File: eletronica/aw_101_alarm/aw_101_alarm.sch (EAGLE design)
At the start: 40 parts, among them IC1 ATTINY2313V, IC2 4511N, J1 DCJ0202, T1 2N2222, T2 2N2222, T3 2N2222, T4 2N2222, T5 2N2222, T6 2N2222, X1 UPDOWN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

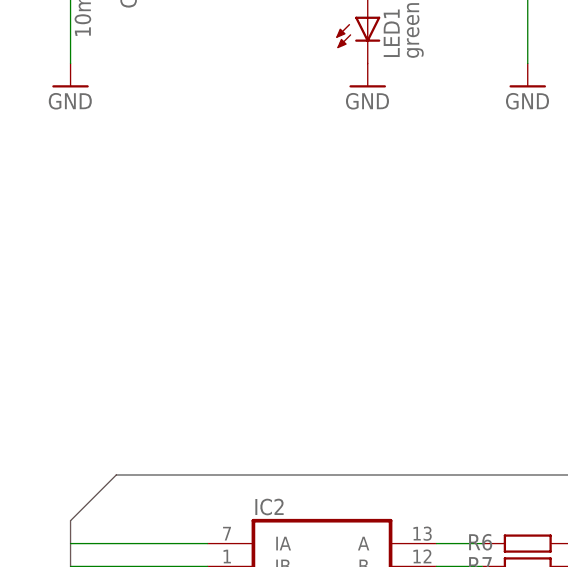
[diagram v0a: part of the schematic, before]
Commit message: 
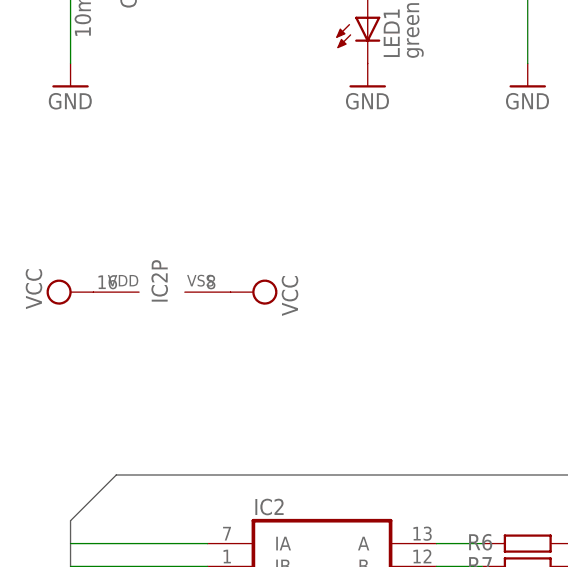
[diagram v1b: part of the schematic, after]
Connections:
- net VCC: now also IC2P.VDD, IC2P.VSS
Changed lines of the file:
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@@
 <part name="R17" library="rcl" deviceset="R-EU_" device="0207/10" value="1K"/>
 <part name="GND9" library="supply1" deviceset="GND" device=""/>
+<part name="SUPPLY3" library="supply2" deviceset="VCC" device=""/>
+<part name="SUPPLY4" library="supply2" deviceset="VCC" device=""/>
 </parts>
 <sheets>
@@
 <instance part="R17" gate="G$1" x="167.64" y="-66.04" rot="R180"/>
 <instance part="GND9" gate="1" x="177.8" y="-86.36"/>
+<instance part="IC2" gate="P" x="10.16" y="17.78" rot="R90"/>
+<instance part="SUPPLY3" gate="G$1" x="0" y="17.78" rot="R90"/>
+<instance part="SUPPLY4" gate="G$1" x="20.32" y="17.78" rot="R270"/>
 </instances>
 <busses>
@@
 <junction x="12.7" y="-22.86"/>
 </segment>
+<segment>
+<pinref part="IC2" gate="P" pin="VDD"/>
+<pinref part="SUPPLY3" gate="G$1" pin="VCC"/>
+</segment>
+<segment>
+<pinref part="IC2" gate="P" pin="VSS"/>
+<pinref part="SUPPLY4" gate="G$1" pin="VCC"/>
+</segment>
 </net>

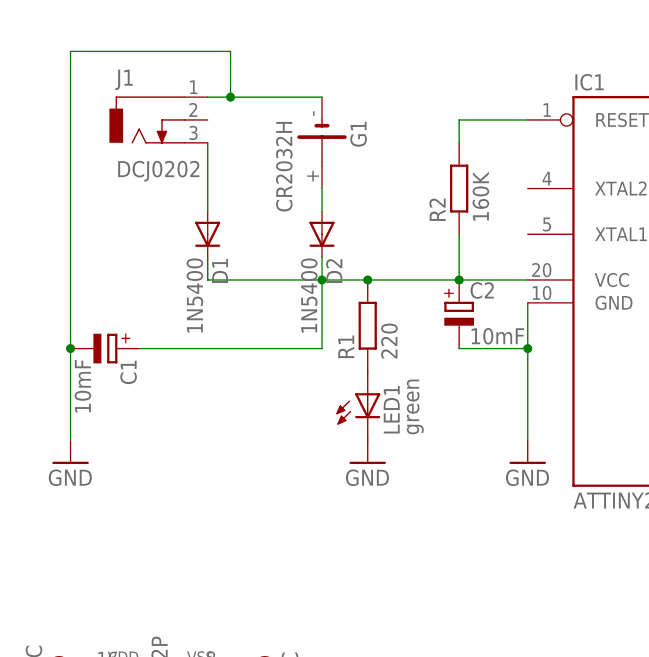
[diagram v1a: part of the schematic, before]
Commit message: 
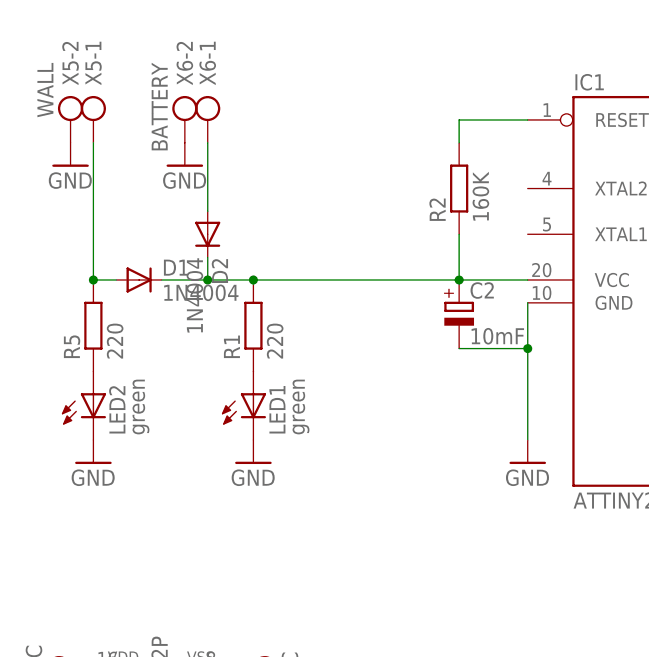
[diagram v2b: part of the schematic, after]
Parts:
- removed C1: 10mF, rcl:CPOL-EUE2.5-6
- removed G1: CR2032H, battery:CR2032H
- removed J1: DCJ0202, con-jack:DCJ0202
- added LED2: green, led:LED5MM
- added R5: 220, rcl:R-EU_0207/10
- added X5: WALL, con-ptr500:AK500/2
- added X6: BATTERY, con-ptr500:AK500/2
- D1, D2: value 1N5400 -> 1N4004; device diode:1N5400 -> diode:1N4004
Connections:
- new net N$37: LED2.A, R5.1
- net GND: now also LED2.C, X5-2.KL, X6-2.KL; no longer C1.-, G1.-, J1.1
- net N$2: now also R5.2, X5-1.KL; no longer J1.3
- net N$3: now also X6-1.KL; no longer G1.+
- net VCC: no longer C1.+
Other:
- moved on the sheet: D1, D2, LED1, R1
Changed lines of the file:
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@@
 </variantdefs>
 <classes>
-<class number="0" name="default" width="0" drill="0">
+<class number="0" name="default" width="1.016" drill="0">
+<clearance class="0" value="1.016"/>
 </class>
 </classes>
 <parts>
-<part name="J1" library="con-jack" deviceset="DCJ0202" device=""/>
-<part name="G1" library="battery" deviceset="CR2032H" device=""/>
-<part name="GND1" library="supply1" deviceset="GND" device=""/>
-<part name="D1" library="diode" deviceset="1N5400" device=""/>
-<part name="D2" library="diode" deviceset="1N5400" device=""/>
-<part name="C1" library="rcl" deviceset="CPOL-EU" device="E2.5-6" value="10mF"/>
 <part name="R1" library="rcl" deviceset="R-EU_" device="0207/10" value="220"/>
 <part name="LED1" library="led" deviceset="LED" device="5MM" value="green"/>
@@
 <part name="SUPPLY3" library="supply2" deviceset="VCC" device=""/>
 <part name="SUPPLY4" library="supply2" deviceset="VCC" device=""/>
+<part name="X5" library="con-ptr500" deviceset="AK500/2" device="" value="WALL"/>
+<part name="GND10" library="supply1" deviceset="GND" device=""/>
+<part name="X6" library="con-ptr500" deviceset="AK500/2" device="" value="BATTERY"/>
+<part name="GND11" library="supply1" deviceset="GND" device=""/>
+<part name="R5" library="rcl" deviceset="R-EU_" device="0207/10" value="220"/>
+<part name="LED2" library="led" deviceset="LED" device="5MM" value="green"/>
+<part name="GND1" library="supply1" deviceset="GND" device=""/>
+<part name="D1" library="diode" deviceset="1N4004" device=""/>
+<part name="D2" library="diode" deviceset="1N4004" device=""/>
 </parts>
 <sheets>
@@
 </plain>
 <instances>
-<instance part="J1" gate="G$1" x="7.62" y="78.74"/>
-<instance part="G1" gate="1" x="27.94" y="76.2" rot="R270"/>
-<instance part="GND1" gate="1" x="0" y="40.64"/>
-<instance part="D1" gate="1" x="15.24" y="66.04" rot="R270"/>
-<instance part="D2" gate="1" x="27.94" y="66.04" rot="R270"/>
-<instance part="C1" gate="G$1" x="5.08" y="53.34" rot="R270"/>
-<instance part="R1" gate="G$1" x="33.02" y="55.88" rot="R90"/>
-<instance part="LED1" gate="G$1" x="33.02" y="48.26"/>
-<instance part="GND2" gate="1" x="33.02" y="40.64"/>
+<instance part="R1" gate="G$1" x="20.32" y="55.88" rot="R90"/>
+<instance part="LED1" gate="G$1" x="20.32" y="48.26"/>
+<instance part="GND2" gate="1" x="20.32" y="40.64"/>
 <instance part="IC1" gate="G$1" x="68.58" y="58.42"/>
 <instance part="R2" gate="G$1" x="43.18" y="71.12" rot="R90"/>
@@
 <instance part="SUPPLY3" gate="G$1" x="0" y="17.78" rot="R90"/>
 <instance part="SUPPLY4" gate="G$1" x="20.32" y="17.78" rot="R270"/>
+<instance part="X5" gate="-1" x="2.54" y="81.28" rot="R270"/>
+<instance part="X5" gate="-2" x="0" y="81.28" rot="R270"/>
+<instance part="GND10" gate="1" x="0" y="73.66"/>
+<instance part="X6" gate="-1" x="15.24" y="81.28" rot="R270"/>
+<instance part="X6" gate="-2" x="12.7" y="81.28" rot="R270"/>
+<instance part="GND11" gate="1" x="12.7" y="73.66"/>
+<instance part="R5" gate="G$1" x="2.54" y="55.88" rot="R90"/>
+<instance part="LED2" gate="G$1" x="2.54" y="48.26"/>
+<instance part="GND1" gate="1" x="2.54" y="40.64"/>
+<instance part="D1" gate="1" x="7.62" y="60.96"/>
+<instance part="D2" gate="1" x="15.24" y="66.04" rot="R270"/>
 </instances>
 <busses>
@@
 <nets>
 <net name="GND" class="0">
-<segment>
-<pinref part="G1" gate="1" pin="-"/>
-<pinref part="J1" gate="G$1" pin="1"/>
-<wire x1="27.94" y1="81.28" x2="17.78" y2="81.28" width="0.1524" layer="91"/>
-<wire x1="17.78" y1="81.28" x2="15.24" y2="81.28" width="0.1524" layer="91"/>
-<wire x1="17.78" y1="81.28" x2="17.78" y2="86.36" width="0.1524" layer="91"/>
-<wire x1="17.78" y1="86.36" x2="0" y2="86.36" width="0.1524" layer="91"/>
-<junction x="17.78" y="81.28"/>
-<pinref part="GND1" gate="1" pin="GND"/>
-<wire x1="0" y1="86.36" x2="0" y2="53.34" width="0.1524" layer="91"/>
-<pinref part="C1" gate="G$1" pin="-"/>
-<wire x1="0" y1="53.34" x2="0" y2="43.18" width="0.1524" layer="91"/>
-<junction x="0" y="53.34"/>
-</segment>
 <segment>
 <pinref part="LED1" gate="G$1" pin="C"/>
@@
 <junction x="101.6" y="-81.28"/>
 </segment>
-</net>
-<net name="N$2" class="0">
-<segment>
-<pinref part="D1" gate="1" pin="A"/>
-<pinref part="J1" gate="G$1" pin="3"/>
-<wire x1="15.24" y1="68.58" x2="15.24" y2="76.2" width="0.1524" layer="91"/>
+<segment>
+<pinref part="X5" gate="-2" pin="KL"/>
+<pinref part="GND10" gate="1" pin="GND"/>
+</segment>
+<segment>
+<pinref part="X6" gate="-2" pin="KL"/>
+<pinref part="GND11" gate="1" pin="GND"/>
+</segment>
+<segment>
+<pinref part="LED2" gate="G$1" pin="C"/>
+<pinref part="GND1" gate="1" pin="GND"/>
 </segment>
 </net>
 <net name="VCC" class="0">
-<segment>
-<pinref part="D1" gate="1" pin="C"/>
-<wire x1="15.24" y1="63.5" x2="15.24" y2="60.96" width="0.1524" layer="91"/>
-<wire x1="15.24" y1="60.96" x2="27.94" y2="60.96" width="0.1524" layer="91"/>
-<pinref part="D2" gate="1" pin="C"/>
-<wire x1="27.94" y1="60.96" x2="33.02" y2="60.96" width="0.1524" layer="91"/>
-<wire x1="27.94" y1="63.5" x2="27.94" y2="60.96" width="0.1524" layer="91"/>
-<junction x="27.94" y="60.96"/>
-<pinref part="C1" gate="G$1" pin="+"/>
-<wire x1="7.62" y1="53.34" x2="27.94" y2="53.34" width="0.1524" layer="91"/>
-<wire x1="27.94" y1="53.34" x2="27.94" y2="60.96" width="0.1524" layer="91"/>
-<pinref part="R1" gate="G$1" pin="2"/>
-<junction x="33.02" y="60.96"/>
-<pinref part="IC1" gate="G$1" pin="VCC"/>
-<wire x1="33.02" y1="60.96" x2="43.18" y2="60.96" width="0.1524" layer="91"/>
-<pinref part="R2" gate="G$1" pin="1"/>
-<wire x1="43.18" y1="60.96" x2="50.8" y2="60.96" width="0.1524" layer="91"/>
-<wire x1="43.18" y1="66.04" x2="43.18" y2="60.96" width="0.1524" layer="91"/>
-<junction x="43.18" y="60.96"/>
-<pinref part="C2" gate="G$1" pin="+"/>
-</segment>
 <segment>
 <pinref part="R4" gate="G$1" pin="2"/>
@@
 <pinref part="SUPPLY4" gate="G$1" pin="VCC"/>
 </segment>
+<segment>
+<pinref part="R1" gate="G$1" pin="2"/>
+<wire x1="15.24" y1="60.96" x2="20.32" y2="60.96" width="0.1524" layer="91"/>
+<wire x1="15.24" y1="63.5" x2="15.24" y2="60.96" width="0.1524" layer="91"/>
+<pinref part="C2" gate="G$1" pin="+"/>
+<wire x1="20.32" y1="60.96" x2="43.18" y2="60.96" width="0.1524" layer="91"/>
+<junction x="20.32" y="60.96"/>
+<pinref part="IC1" gate="G$1" pin="VCC"/>
+<wire x1="43.18" y1="60.96" x2="50.8" y2="60.96" width="0.1524" layer="91"/>
+<junction x="43.18" y="60.96"/>
+<pinref part="R2" gate="G$1" pin="1"/>
+<wire x1="43.18" y1="60.96" x2="43.18" y2="66.04" width="0.1524" layer="91"/>
+<pinref part="D2" gate="1" pin="C"/>
+<pinref part="D1" gate="1" pin="C"/>
+<wire x1="10.16" y1="60.96" x2="15.24" y2="60.96" width="0.1524" layer="91"/>
+<junction x="15.24" y="60.96"/>
+</segment>
 </net>
 <net name="N$4" class="0">
@@
 <net name="N$3" class="0">
 <segment>
-<pinref part="G1" gate="1" pin="+"/>
+<pinref part="X6" gate="-1" pin="KL"/>
+<wire x1="15.24" y1="76.2" x2="15.24" y2="68.58" width="0.1524" layer="91"/>
 <pinref part="D2" gate="1" pin="A"/>
-<wire x1="27.94" y1="68.58" x2="27.94" y2="71.12" width="0.1524" layer="91"/>
 </segment>
 </net>
@@
 </segment>
 </net>
+<net name="N$37" class="0">
+<segment>
+<pinref part="R5" gate="G$1" pin="1"/>
+<pinref part="LED2" gate="G$1" pin="A"/>
+</segment>
+</net>
+<net name="N$2" class="0">
+<segment>
+<pinref part="X5" gate="-1" pin="KL"/>
+<pinref part="R5" gate="G$1" pin="2"/>
+<wire x1="2.54" y1="76.2" x2="2.54" y2="60.96" width="0.1524" layer="91"/>
+<pinref part="D1" gate="1" pin="A"/>
+<wire x1="2.54" y1="60.96" x2="5.08" y2="60.96" width="0.1524" layer="91"/>
+<junction x="2.54" y="60.96"/>
+</segment>
+</net>

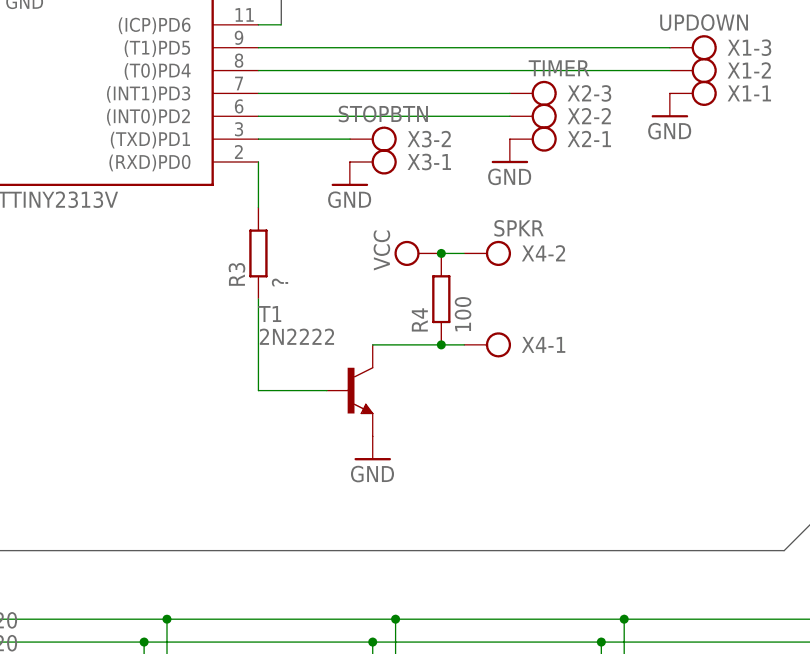
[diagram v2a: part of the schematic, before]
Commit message: 
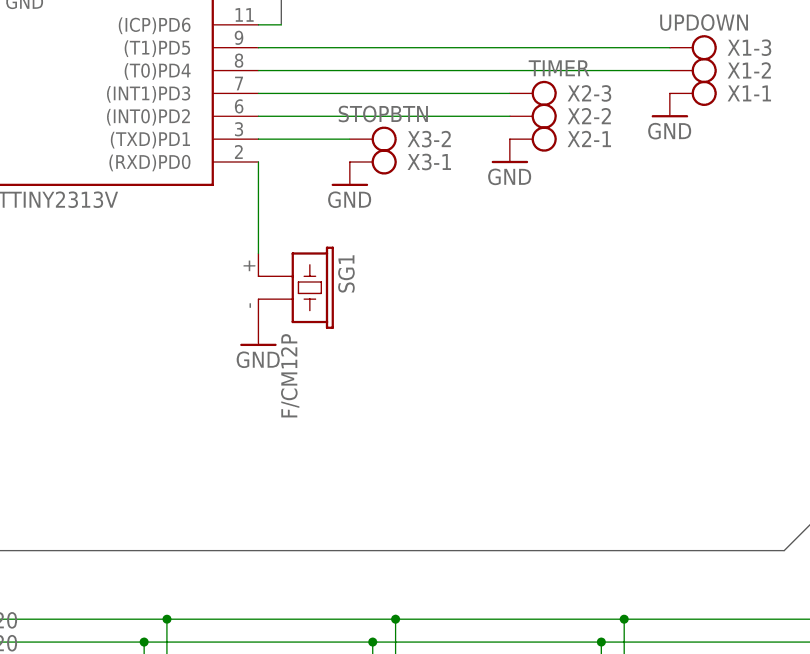
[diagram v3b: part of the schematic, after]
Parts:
- removed R3: ?, rcl:R-EU_0207/10
- removed R4: 100, rcl:R-EU_0207/10
- removed T1: 2N2222, transistor:2N2222
- removed X4: SPKR, con-ptr500:AK500/2
- added SG1: F/CM12P, buzzer:F/CM12P
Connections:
- removed net N$11: R3.1, T1.B
- removed net N$12: R4.1, T1.C, X4-1.KL
- net GND: now also SG1.2; no longer T1.E
- net N$10: now also SG1.1; no longer R3.2
- net VCC: no longer R4.2, X4-2.KL
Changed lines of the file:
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@@
 <part name="X3" library="con-ptr500" deviceset="AK500/2" device="" value="STOPBTN"/>
 <part name="GND6" library="supply1" deviceset="GND" device=""/>
-<part name="R3" library="rcl" deviceset="R-EU_" device="0207/10" value="?"/>
-<part name="T1" library="transistor" deviceset="2N2222" device=""/>
-<part name="GND7" library="supply1" deviceset="GND" device=""/>
-<part name="X4" library="con-ptr500" deviceset="AK500/2" device="" value="SPKR"/>
-<part name="R4" library="rcl" deviceset="R-EU_" device="0207/10" value="100"/>
-<part name="SUPPLY1" library="supply2" deviceset="VCC" device=""/>
 <part name="C2" library="rcl" deviceset="CPOL-EU" device="E2.5-6" value="10mF"/>
 <part name="IC2" library="45xx" deviceset="4511" device="N"/>
@@
 <part name="D1" library="diode" deviceset="1N4004" device=""/>
 <part name="D2" library="diode" deviceset="1N4004" device=""/>
+<part name="SG1" library="buzzer" deviceset="F/CM12P" device=""/>
+<part name="GND7" library="supply1" deviceset="GND" device=""/>
 </parts>
 <sheets>
@@
 <instance part="X3" gate="-2" x="101.6" y="43.18" rot="R180"/>
 <instance part="GND6" gate="1" x="96.52" y="38.1"/>
-<instance part="R3" gate="G$1" x="86.36" y="30.48" rot="R90"/>
-<instance part="T1" gate="G$1" x="96.52" y="15.24"/>
-<instance part="GND7" gate="1" x="99.06" y="7.62"/>
-<instance part="X4" gate="-1" x="114.3" y="20.32" rot="R180"/>
-<instance part="X4" gate="-2" x="114.3" y="30.48" rot="R180"/>
-<instance part="R4" gate="G$1" x="106.68" y="25.4" rot="R90"/>
-<instance part="SUPPLY1" gate="G$1" x="104.14" y="30.48" rot="R90"/>
 <instance part="C2" gate="G$1" x="43.18" y="58.42"/>
 <instance part="IC2" gate="A" x="27.94" y="-17.78"/>
@@
 <instance part="D1" gate="1" x="7.62" y="60.96"/>
 <instance part="D2" gate="1" x="15.24" y="66.04" rot="R270"/>
+<instance part="SG1" gate="G$1" x="88.9" y="27.94" rot="R270"/>
+<instance part="GND7" gate="1" x="86.36" y="20.32"/>
 </instances>
 <busses>
@@
 <pinref part="X3" gate="-1" pin="KL"/>
 <pinref part="GND6" gate="1" pin="GND"/>
-</segment>
-<segment>
-<pinref part="T1" gate="G$1" pin="E"/>
-<pinref part="GND7" gate="1" pin="GND"/>
 </segment>
 <segment>
@@
 <pinref part="GND1" gate="1" pin="GND"/>
 </segment>
+<segment>
+<pinref part="SG1" gate="G$1" pin="2"/>
+<pinref part="GND7" gate="1" pin="GND"/>
+</segment>
 </net>
 <net name="VCC" class="0">
-<segment>
-<pinref part="R4" gate="G$1" pin="2"/>
-<pinref part="SUPPLY1" gate="G$1" pin="VCC"/>
-<pinref part="X4" gate="-2" pin="KL"/>
-<wire x1="106.68" y1="30.48" x2="109.22" y2="30.48" width="0.1524" layer="91"/>
-<junction x="106.68" y="30.48"/>
-</segment>
 <segment>
 <pinref part="IC2" gate="A" pin="LT"/>
@@
 <pinref part="IC1" gate="G$1" pin="(TXD)PD1"/>
 <wire x1="96.52" y1="43.18" x2="86.36" y2="43.18" width="0.1524" layer="91"/>
-</segment>
-</net>
-<net name="N$10" class="0">
-<segment>
-<pinref part="IC1" gate="G$1" pin="(RXD)PD0"/>
-<pinref part="R3" gate="G$1" pin="2"/>
-<wire x1="86.36" y1="40.64" x2="86.36" y2="35.56" width="0.1524" layer="91"/>
-</segment>
-</net>
-<net name="N$11" class="0">
-<segment>
-<pinref part="R3" gate="G$1" pin="1"/>
-<pinref part="T1" gate="G$1" pin="B"/>
-<wire x1="86.36" y1="25.4" x2="86.36" y2="15.24" width="0.1524" layer="91"/>
-<wire x1="86.36" y1="15.24" x2="93.98" y2="15.24" width="0.1524" layer="91"/>
-</segment>
-</net>
-<net name="N$12" class="0">
-<segment>
-<pinref part="T1" gate="G$1" pin="C"/>
-<pinref part="X4" gate="-1" pin="KL"/>
-<wire x1="99.06" y1="20.32" x2="106.68" y2="20.32" width="0.1524" layer="91"/>
-<pinref part="R4" gate="G$1" pin="1"/>
-<wire x1="106.68" y1="20.32" x2="109.22" y2="20.32" width="0.1524" layer="91"/>
-<junction x="106.68" y="20.32"/>
 </segment>
 </net>
@@
 </segment>
 </net>
+<net name="N$10" class="0">
+<segment>
+<pinref part="IC1" gate="G$1" pin="(RXD)PD0"/>
+<pinref part="SG1" gate="G$1" pin="1"/>
+<wire x1="86.36" y1="40.64" x2="86.36" y2="30.48" width="0.1524" layer="91"/>
+</segment>
+</net>
